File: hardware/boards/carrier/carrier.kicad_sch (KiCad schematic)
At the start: 0 parts

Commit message: Checkpoint
_sigh_
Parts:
- added J1: XT30PW(2+2)-M.G.B_SLOT, mini-rack-power:Amass_XT30PW_2plus2_M_RightAngle_THT, symbol Connector_Generic:Conn_01x04
- added J2: DC_IN+_OUT, Connector_PinHeader_2.54mm:PinHeader_1x01_P2.54mm_Vertical, symbol Connector_Generic:Conn_01x01
- added J3: GND_OUT, Connector_PinHeader_2.54mm:PinHeader_1x01_P2.54mm_Vertical, symbol Connector_Generic:Conn_01x01
- added J4: I2C_OUT, Connector_PinHeader_2.54mm:PinHeader_1x02_P2.54mm_Vertical, symbol Connector_Generic:Conn_01x02
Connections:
- new net DC_IN+: J1.1 (Pin_1), J2.1 (Pin_1)
- new net GND: J1.2 (Pin_2), J3.1 (Pin_1)
- new net SCL: J1.4 (Pin_4), J4.2 (Pin_2)
- new net SDA: J1.3 (Pin_3), J4.1 (Pin_1)
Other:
- note added: "Carrier-side XT30 pin assumption follows backplane: 1=DC_IN+, 2=GND, 3=SDA, 4=SCL. Verify against final mating connector documentation before fab."

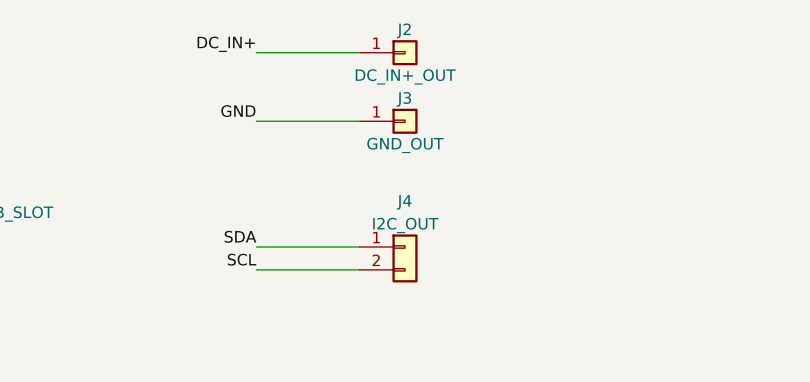
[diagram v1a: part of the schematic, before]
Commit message: Use 1x2 headers on carrier outputs
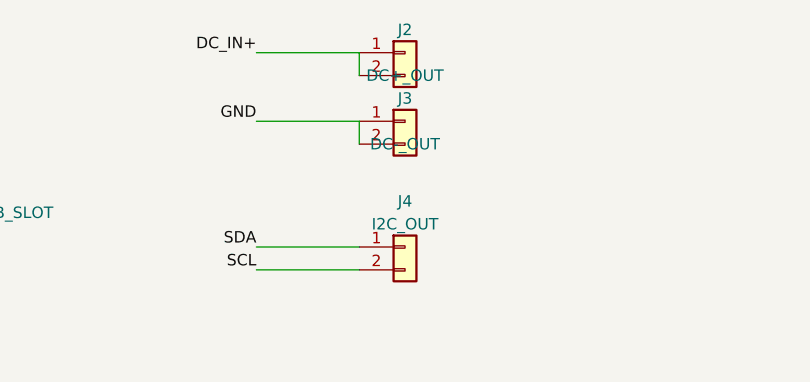
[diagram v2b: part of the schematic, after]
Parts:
- J2: value DC_IN+_OUT -> DC+_OUT; footprint Connector_PinHeader_2.54mm:PinHeader_1x01_P2.54mm_Vertical -> Connector_PinHeader_2.54mm:PinHeader_1x02_P2.54mm_Vertical; symbol Connector_Generic:Conn_01x01 -> Connector_Generic:Conn_01x02
- J3: value GND_OUT -> DC-_OUT; footprint Connector_PinHeader_2.54mm:PinHeader_1x01_P2.54mm_Vertical -> Connector_PinHeader_2.54mm:PinHeader_1x02_P2.54mm_Vertical; symbol Connector_Generic:Conn_01x01 -> Connector_Generic:Conn_01x02
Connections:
- net DC_IN+: now also J2.2 (Pin_2)
- net GND: now also J3.2 (Pin_2)
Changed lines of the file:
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@@
+	(wire
+		(pts
+			(xy 130.81 43.18) (xy 130.81 45.72)
+		)
+		(stroke
+			(width 0)
+			(type default)
+		)
+	)
 	(wire
 		(pts
 			(xy 119.38 50.8) (xy 130.81 50.8)
+		)
+		(stroke
+			(width 0)
+			(type default)
+		)
+	)
+	(wire
+		(pts
+			(xy 130.81 50.8) (xy 130.81 53.34)
 		)
 		(stroke
@@
 	)
 	(symbol
-		(lib_id "Connector_Generic:Conn_01x01")
+		(lib_id "Connector_Generic:Conn_01x02")
 		(at 135.89 43.18 0)
 		(unit 1)
@@
 			)
 		)
-		(property "Value" "DC_IN+_OUT"
+		(property "Value" "DC+_OUT"
 			(at 135.89 45.72 0)
 			(show_name no)
@@
 			)
 		)
-		(property "Footprint" "Connector_PinHeader_2.54mm:PinHeader_1x01_P2.54mm_Vertical"
+		(property "Footprint" "Connector_PinHeader_2.54mm:PinHeader_1x02_P2.54mm_Vertical"
 			(at 135.89 43.18 0)
 			(hide yes)
@@
 			)
 		)
-		(property "Description" "Single-pin breakout for carrier DC input positive"
+		(property "Description" "Two-pin breakout for carrier DC input positive"
 			(at 135.89 43.18 0)
 			(hide yes)
@@
 		)
 		(pin "1"
+		)
+		(pin "2"
 		)
 		(instances
@@
 	)
 	(symbol
-		(lib_id "Connector_Generic:Conn_01x01")
+		(lib_id "Connector_Generic:Conn_01x02")
 		(at 135.89 50.8 0)
 		(unit 1)
@@
 			)
 		)
-		(property "Value" "GND_OUT"
+		(property "Value" "DC-_OUT"
 			(at 135.89 53.34 0)
 			(show_name no)
@@
 			)
 		)
-		(property "Footprint" "Connector_PinHeader_2.54mm:PinHeader_1x01_P2.54mm_Vertical"
+		(property "Footprint" "Connector_PinHeader_2.54mm:PinHeader_1x02_P2.54mm_Vertical"
 			(at 135.89 50.8 0)
 			(hide yes)
@@
 			)
 		)
-		(property "Description" "Single-pin breakout for carrier DC input return"
+		(property "Description" "Two-pin breakout for carrier DC input return"
 			(at 135.89 50.8 0)
 			(hide yes)
@@
 		(pin "1"
 		)
+		(pin "2"
+		)
 		(instances

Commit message: chore: checkpoint current project updates
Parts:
- J4: value I2C_OUT -> I2C_IQR_OUT; footprint Connector_PinHeader_2.54mm:PinHeader_1x02_P2.54mm_Vertical -> Connector_PinHeader_2.54mm:PinHeader_1x03_P2.54mm_Vertical; symbol Connector_Generic:Conn_01x02 -> Connector_Generic:Conn_01x03
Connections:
- net SDA: now also J4.3 (Pin_3); no longer J4.1 (Pin_1)
- no-connect marks 0 -> 1
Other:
- note added: "IQR (NC)"
- moved on the sheet: J2, J3
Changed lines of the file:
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@@
 		(rev "A")
 	)
-	(text "Carrier-side XT30 pin assumption follows backplane: 1=DC_IN+, 2=GND, 3=SDA, 4=SCL. Verify against final mating connector documentation before fab."
+	(text "Carrier-side XT30 pin assumption follows backplane: \n\n1=DC_IN+, 2=GND, 3=SDA, 4=SCL. \n\nVerify against final mating connector documentation before fab."
 		(exclude_from_sim no)
 		(at 35.56 82.55 0)
 		(effects
 			(font
-				(size 1.27 1.27)
+				(face "JetBrainsMono NF")
+				(size 1.27 1.27)
+				(bold yes)
 			)
 			(justify left bottom)
 		)
 	)
+	(text "IQR (NC)"
+		(exclude_from_sim no)
+		(at 110.49 59.69 0)
+		(effects
+			(font
+				(size 1.27 1.27)
+			)
+			(justify right bottom)
+		)
+	)
+	(junction
+		(at 121.92 39.37)
+		(diameter 0)
+		(color 0 0 0 0)
+	)
+	(junction
+		(at 121.92 50.8)
+		(diameter 0)
+		(color 0 0 0 0)
+	)
+	(no_connect
+		(at 121.92 59.69)
+	)
 	(wire
 		(pts
@@
 	(wire
 		(pts
-			(xy 119.38 43.18) (xy 130.81 43.18)
-		)
-		(stroke
-			(width 0)
-			(type default)
-		)
-	)
-	(wire
-		(pts
-			(xy 130.81 43.18) (xy 130.81 45.72)
-		)
-		(stroke
-			(width 0)
-			(type default)
-		)
-	)
-	(wire
-		(pts
-			(xy 119.38 50.8) (xy 130.81 50.8)
-		)
-		(stroke
-			(width 0)
-			(type default)
-		)
-	)
-	(wire
-		(pts
-			(xy 130.81 50.8) (xy 130.81 53.34)
-		)
-		(stroke
-			(width 0)
-			(type default)
-		)
-	)
-	(wire
-		(pts
-			(xy 119.38 64.77) (xy 130.81 64.77)
-		)
-		(stroke
-			(width 0)
-			(type default)
-		)
-	)
-	(wire
-		(pts
-			(xy 119.38 67.31) (xy 130.81 67.31)
+			(xy 110.49 39.37) (xy 121.92 39.37)
+		)
+		(stroke
+			(width 0)
+			(type default)
+		)
+	)
+	(wire
+		(pts
+			(xy 110.49 50.8) (xy 121.92 50.8)
+		)
+		(stroke
+			(width 0)
+			(type default)
+		)
+	)
+	(wire
+		(pts
+			(xy 110.49 62.23) (xy 121.92 62.23)
+		)
+		(stroke
+			(width 0)
+			(type default)
+		)
+	)
+	(wire
+		(pts
+			(xy 110.49 64.77) (xy 121.92 64.77)
+		)
+		(stroke
+			(width 0)
+			(type default)
+		)
+	)
+	(wire
+		(pts
+			(xy 121.92 39.37) (xy 121.92 41.91)
+		)
+		(stroke
+			(width 0)
+			(type default)
+		)
+	)
+	(wire
+		(pts
+			(xy 121.92 50.8) (xy 121.92 53.34)
 		)
 		(stroke
@@
 	)
 	(label "DC_IN+"
-		(at 119.38 43.18 180)
+		(at 110.49 39.37 180)
 		(effects
 			(font
@@
 	)
 	(label "GND"
-		(at 119.38 50.8 180)
+		(at 110.49 50.8 180)
+		(effects
+			(font
+				(size 1.27 1.27)
+			)
+			(justify right bottom)
+		)
+	)
+	(label "SCL"
+		(at 110.49 62.23 180)
 		(effects
 			(font
@@
 	)
 	(label "SDA"
-		(at 119.38 64.77 180)
-		(effects
-			(font
-				(size 1.27 1.27)
-			)
-			(justify right bottom)
-		)
-	)
-	(label "SCL"
-		(at 119.38 67.31 180)
+		(at 110.49 64.77 180)
 		(effects
 			(font
@@
 	(symbol
 		(lib_id "Connector_Generic:Conn_01x02")
-		(at 135.89 43.18 0)
+		(at 127 39.37 0)
 		(unit 1)
 		(body_style 1)
@@
 		(dnp no)
 		(property "Reference" "J2"
-			(at 135.89 40.64 0)
+			(at 127 36.83 0)
 			(show_name no)
 			(do_not_autoplace no)
@@
 		)
 		(property "Value" "DC+_OUT"
-			(at 135.89 45.72 0)
+			(at 127 44.958 0)
 			(show_name no)
 			(do_not_autoplace no)
@@
 		)
 		(property "Footprint" "Connector_PinHeader_2.54mm:PinHeader_1x02_P2.54mm_Vertical"
-			(at 135.89 43.18 0)
+			(at 127 39.37 0)
 			(hide yes)
 			(show_name no)
@@
 		)
 		(property "Datasheet" ""
-			(at 135.89 43.18 0)
+			(at 127 39.37 0)
 			(hide yes)
 			(show_name no)
@@
 		)
 		(property "Description" "Two-pin breakout for carrier DC input positive"
-			(at 135.89 43.18 0)
+			(at 127 39.37 0)
 			(hide yes)
 			(show_name no)
@@
 	(symbol
 		(lib_id "Connector_Generic:Conn_01x02")
-		(at 135.89 50.8 0)
+		(at 127 50.8 0)
 		(unit 1)
 		(body_style 1)
@@
 		(dnp no)
 		(property "Reference" "J3"
-			(at 135.89 48.26 0)
+			(at 127 48.26 0)
 			(show_name no)
 			(do_not_autoplace no)
@@
 		)
 		(property "Value" "DC-_OUT"
-			(at 135.89 53.34 0)
+			(at 127 56.388 0)
 			(show_name no)
 			(do_not_autoplace no)
@@
 		)
 		(property "Footprint" "Connector_PinHeader_2.54mm:PinHeader_1x02_P2.54mm_Vertical"
-			(at 135.89 50.8 0)
+			(at 127 50.8 0)
 			(hide yes)
 			(show_name no)
@@
 		)
 		(property "Datasheet" ""
-			(at 135.89 50.8 0)
+			(at 127 50.8 0)
 			(hide yes)
 			(show_name no)
@@
 		)
 		(property "Description" "Two-pin breakout for carrier DC input return"
-			(at 135.89 50.8 0)
+			(at 127 50.8 0)
 			(hide yes)
 			(show_name no)
@@
 	)
 	(symbol
-		(lib_id "Connector_Generic:Conn_01x02")
-		(at 135.89 64.77 0)
+		(lib_id "Connector_Generic:Conn_01x03")
+		(at 127 62.23 0)
 		(unit 1)
 		(body_style 1)
@@
 		(dnp no)
 		(property "Reference" "J4"
-			(at 135.89 59.69 0)
-			(show_name no)
-			(do_not_autoplace no)
-			(effects
-				(font
-					(size 1.27 1.27)
-				)
-			)
-		)
-		(property "Value" "I2C_OUT"
-			(at 135.89 62.23 0)
-			(show_name no)
-			(do_not_autoplace no)
-			(effects
-				(font
-					(size 1.27 1.27)
-				)
-			)
-		)
-		(property "Footprint" "Connector_PinHeader_2.54mm:PinHeader_1x02_P2.54mm_Vertical"
-			(at 135.89 64.77 0)
+			(at 126.746 59.436 0)
+			(show_name no)
+			(do_not_autoplace no)
+			(effects
+				(font
+					(size 1.27 1.27)
+				)
+			)
+		)
+		(property "Value" "I2C_IQR_OUT"
+			(at 127 68.834 0)
+			(show_name no)
+			(do_not_autoplace no)
+			(effects
+				(font
+					(size 1.27 1.27)
+				)
+			)
+		)
+		(property "Footprint" "Connector_PinHeader_2.54mm:PinHeader_1x03_P2.54mm_Vertical"
+			(at 127 62.23 0)
 			(hide yes)
 			(show_name no)
@@
 		)
 		(property "Datasheet" ""
-			(at 135.89 64.77 0)
-			(hide yes)
-			(show_name no)
-			(do_not_autoplace no)
-			(effects
-				(font
-					(size 1.27 1.27)
-				)
-			)
-		)
-		(property "Description" "Two-pin breakout for carrier I2C bus"
-			(at 135.89 64.77 0)
+			(at 127 62.23 0)
+			(hide yes)
+			(show_name no)
+			(do_not_autoplace no)
+			(effects
+				(font
+					(size 1.27 1.27)
+				)
+			)
+		)
+		(property "Description" "Three-pin breakout for carrier I2C bus with reserved IQR"
+			(at 127 62.23 0)
 			(hide yes)
 			(show_name no)
@@
 		(pin "2"
 		)
+		(pin "3"
+		)
 		(instances

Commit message: chore: add placeholder part source properties
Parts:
- J1, J2, J3, J4: Part_source (none) -> LCSC,XXXXXXX
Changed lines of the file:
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@@
+			)
+		)
+		(property "Part_source" "LCSC,XXXXXXX"
+			(at 85.09 50.8 0)
+			(hide yes)
+			(show_name no)
+			(do_not_autoplace no)
+			(effects
+				(font
+					(size 1.27 1.27)
+				)
 			)
 		)
@@
 			)
 		)
+		(property "Part_source" "LCSC,XXXXXXX"
+			(at 127 39.37 0)
+			(hide yes)
+			(show_name no)
+			(do_not_autoplace no)
+			(effects
+				(font
+					(size 1.27 1.27)
+				)
+			)
+		)
 		(pin "1"
 		)
@@
 			)
 		)
+		(property "Part_source" "LCSC,XXXXXXX"
+			(at 127 50.8 0)
+			(hide yes)
+			(show_name no)
+			(do_not_autoplace no)
+			(effects
+				(font
+					(size 1.27 1.27)
+				)
+			)
+		)
 		(pin "1"
 		)
@@
 			(at 127 62.23 0)
 			(hide yes)
+			(show_name no)
+			(do_not_autoplace no)
+			(effects
+				(font
+					(size 1.27 1.27)
+				)
+			)
+		)
+		(property "Part_source" "LCSC,XXXXXXX"
+			(at 127 62.23 0)
+			(hide yes)

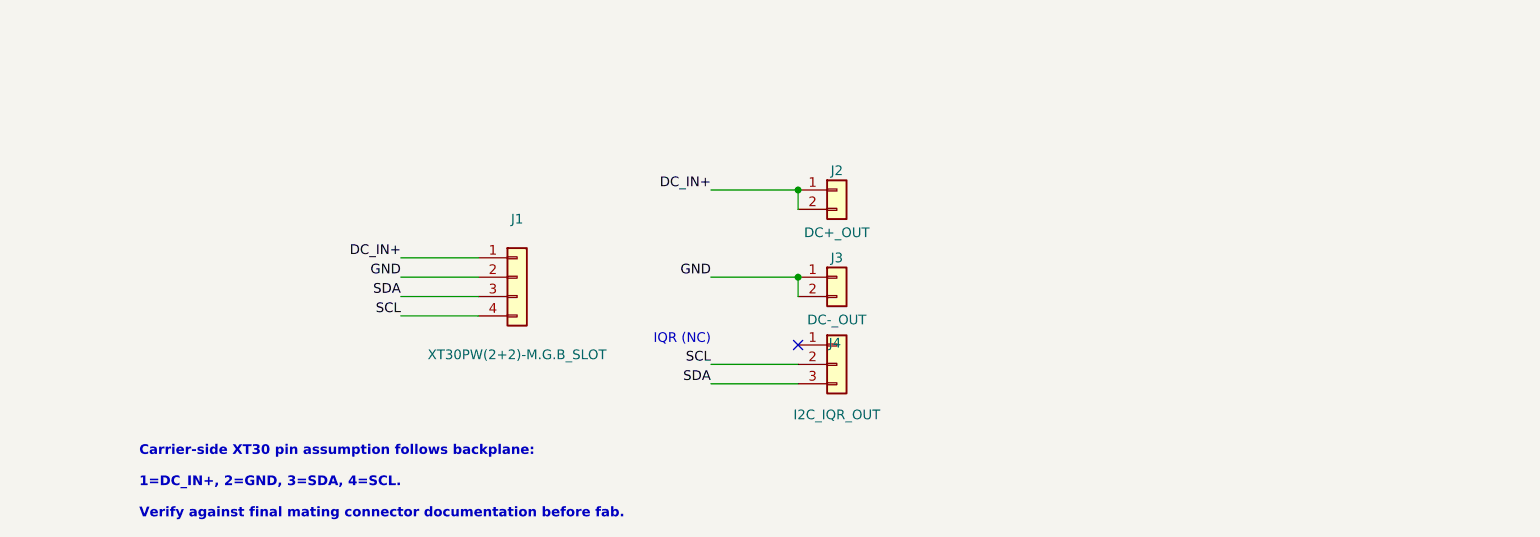
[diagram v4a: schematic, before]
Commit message: fix carrier sw3538 footprint alignment
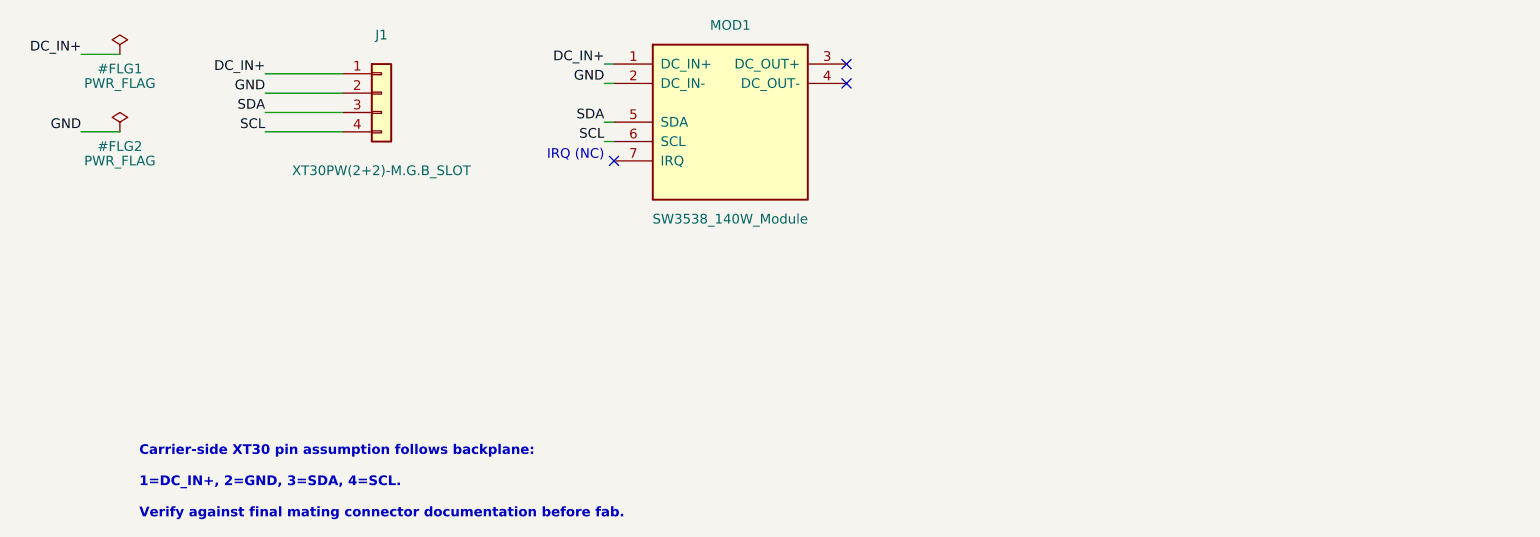
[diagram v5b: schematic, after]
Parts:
- removed J3: DC-_OUT, Connector_PinHeader_2.54mm:PinHeader_1x02_P2.54mm_Vertical, symbol Connector_Generic:Conn_01x02
- removed J4: I2C_IQR_OUT, Connector_PinHeader_2.54mm:PinHeader_1x03_P2.54mm_Vertical, symbol Connector_Generic:Conn_01x03
- MOD1: renamed from J2; value DC+_OUT -> SW3538_140W_Module; footprint Connector_PinHeader_2.54mm:PinHeader_1x02_P2.54mm_Vertical -> mini-rack-power:SW3538_140W_Module; symbol Connector_Generic:Conn_01x02 -> mini-rack-power:SW3538_140W_Module; Part_source LCSC,XXXXXXX -> AliExpress:3256808659168317
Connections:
- net DC_IN+: no longer MOD1.2 (Pin_2)
- net GND: now also MOD1.2 (DC_IN-)
- net SCL: now also MOD1.6 (SCL)
- net SDA: now also MOD1.5 (SDA)
- no-connect marks 1 -> 3
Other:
- note added: "IRQ (NC)"
- note removed: "IQR (NC)"
- moved on the sheet: J1

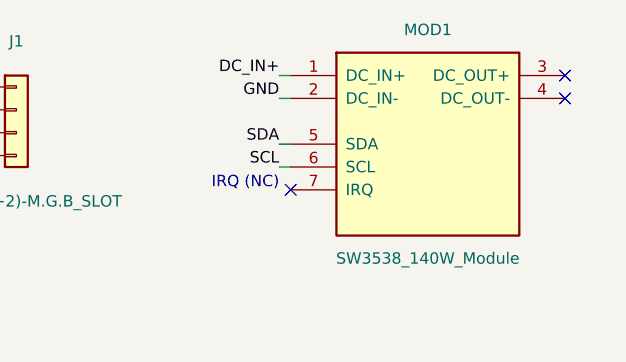
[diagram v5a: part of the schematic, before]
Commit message: Capture manual XT30 corrections
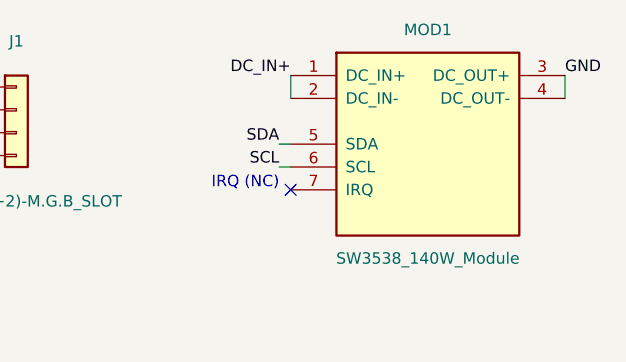
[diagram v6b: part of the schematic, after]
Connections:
- net DC_IN+: now also MOD1.2 (DC_IN-)
- net GND: now also MOD1.3 (DC_OUT+), MOD1.4 (DC_OUT-); no longer MOD1.2 (DC_IN-)
- no-connect marks 3 -> 1
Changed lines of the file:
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@@
 		(at 97.79 35.56)
-	)
-	(no_connect
-		(at 128.27 22.86)
-	)
-	(no_connect
-		(at 128.27 25.4)
 	)
 	(wire
@@
 	(wire
 		(pts
-			(xy 96.52 22.86) (xy 97.79 22.86)
+			(xy 97.79 22.86) (xy 97.79 25.4)
 		)
 		(stroke
@@
 	(wire
 		(pts
-			(xy 96.52 25.4) (xy 97.79 25.4)
+			(xy 128.27 22.86) (xy 128.27 25.4)
 		)
 		(stroke
@@
 	)
 	(label "DC_IN+"
-		(at 96.52 22.86 180)
+		(at 97.79 22.86 180)
 		(effects
 			(font
@@
 	)
 	(label "GND"
-		(at 96.52 25.4 180)
+		(at 128.27 22.86 0)
 		(effects
 			(font
 				(size 1.27 1.27)
 			)
-			(justify right bottom)
+			(justify left bottom)
 		)
 	)

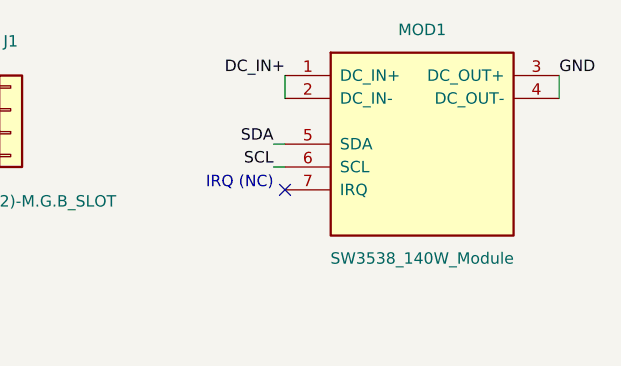
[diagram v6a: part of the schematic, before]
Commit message: Route carrier PCB and generate fabrication package
Correct the SW3538 paired DC input and ground pin mapping. Add carrier routing, copper fill, board identification, and OSHW branding, then include the Fabrication Toolkit configuration and generated production outputs.
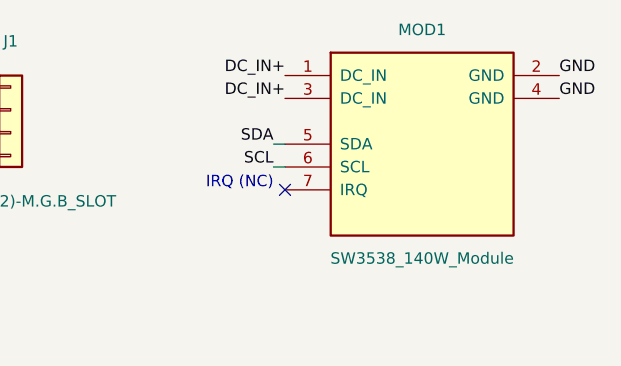
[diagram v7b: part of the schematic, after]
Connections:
- net DC_IN+: now also MOD1.3 (DC_IN); no longer MOD1.2 (DC_IN-)
- net GND: now also MOD1.2 (GND); no longer MOD1.3 (DC_OUT+)
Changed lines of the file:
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@@
-		)
-	)
-	(wire
-		(pts
-			(xy 97.79 22.86) (xy 97.79 25.4)
-		)
-		(stroke
-			(width 0)
-			(type default)
-		)
-	)
-	(wire
-		(pts
-			(xy 128.27 22.86) (xy 128.27 25.4)
-		)
-		(stroke
-			(width 0)
-			(type default)
 		)
 	)
@@
 	)
 	(label "GND"
+		(at 128.27 25.4 0)
+		(effects
+			(font
+				(size 1.27 1.27)
+			)
+			(justify left bottom)
+		)
+	)
+	(label "GND"
 		(at 128.27 22.86 0)
 		(effects
@@
 			)
 			(justify left bottom)
+		)
+	)
+	(label "DC_IN+"
+		(at 97.79 25.4 180)
+		(effects
+			(font
+				(size 1.27 1.27)
+			)
+			(justify right bottom)
 		)
 	)
@@
 		)
 		(property "Description" "SW3538 140W USB-C/PD module with DC input/output, I2C, and IRQ"
-			(at 113.03 50.8 0)
-			(hide yes)
-			(show_name no)
+			(at 113.03 52.832 0)
+			(hide yes)
+			(show_name no)
